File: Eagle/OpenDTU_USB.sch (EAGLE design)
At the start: 6 parts, among them M2 WIRELESS-NRF24L01-PA-EXT, X1 USBPCB

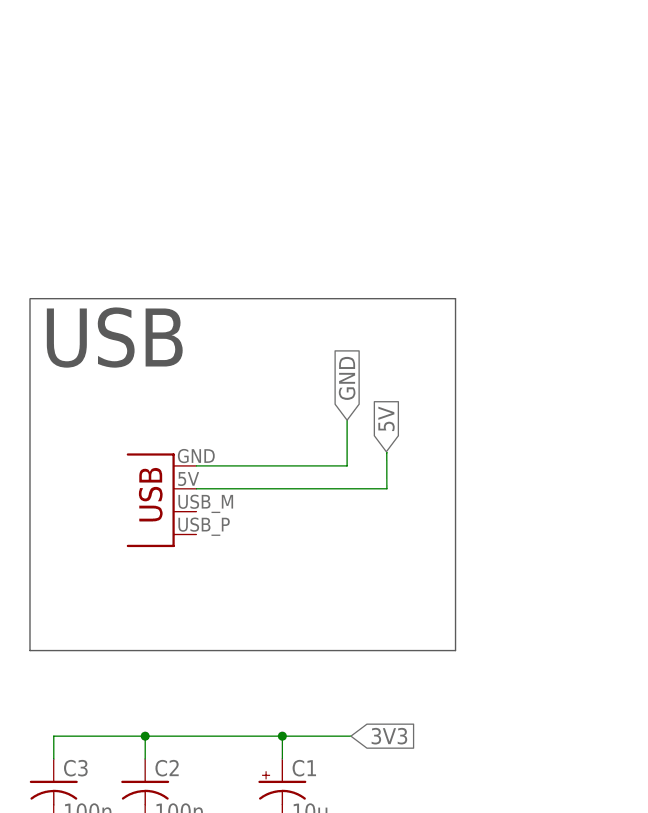
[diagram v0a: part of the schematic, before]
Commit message: Schraubklemme hinzugefügt, Empfang verbessert, USB wegbrechbar
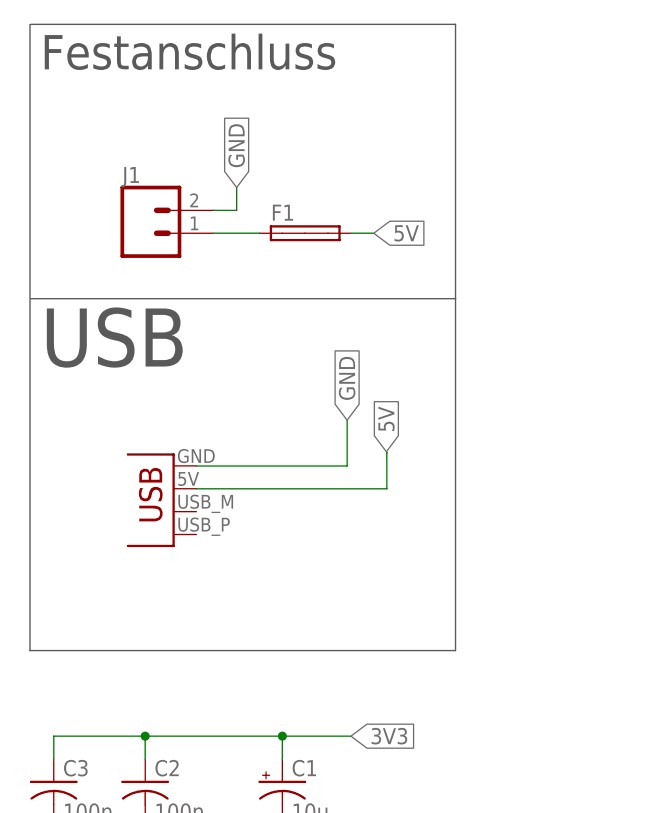
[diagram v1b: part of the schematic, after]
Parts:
- added F1: (no value), fuse:SHK20L
- added J1: (no value), SparkFun-Connectors:CONN_025MM
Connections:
- new net N$2: F1.1A, J1.1
- net 5V: now also F1.2A
- net GND: now also J1.2
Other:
- note added: "Festanschluss"
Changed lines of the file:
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@@
 <part name="C3" library="adafruit" library_urn="urn:adsk.eagle:library:420" deviceset="C-US" device="C0805K" package3d_urn="urn:adsk.eagle:package:6240397/1" value="100n"/>
 <part name="FRAME1" library="SparkFun-Aesthetics" library_urn="urn:adsk.eagle:library:507" deviceset="FRAME-A4L" device=""/>
+<part name="J1" library="SparkFun-Connectors" library_urn="urn:adsk.eagle:library:513" deviceset="CONN_02" device="5MM" package3d_urn="urn:adsk.eagle:package:38044/1"/>
+<part name="F1" library="fuse" library_urn="urn:adsk.eagle:library:233" deviceset="SHK20L" device="" package3d_urn="urn:adsk.eagle:package:14071/1"/>
 </parts>
 <sheets>
@@
 <wire x1="44.6428" y1="63.85" x2="44.6428" y2="24.75" width="0.1524" layer="97"/>
 <wire x1="44.6428" y1="24.75" x2="-2.64" y2="24.75" width="0.1524" layer="97"/>
-<wire x1="-2.64" y1="24.75" x2="-2.64" y2="63.84" width="0.1524" layer="97"/>
+<wire x1="-2.64" y1="24.75" x2="-2.64" y2="94.32" width="0.1524" layer="97"/>
 <text x="-1.46" y="56.31" size="6.4516" layer="97">USB</text>
+<wire x1="-2.53" y1="94.33" x2="44.6428" y2="94.33" width="0.1524" layer="97"/>
+<wire x1="44.6428" y1="94.33" x2="44.6428" y2="63.85" width="0.1524" layer="97"/>
+<text x="-1.46" y="89.33" size="3.81" layer="97">Festanschluss</text>
 </plain>
 <instances>
@@
 <attribute name="LAST_DATE_TIME" x="171.45" y="-77.47" size="2.286" layer="94" font="vector"/>
 <attribute name="SHEET" x="185.42" y="-82.55" size="2.54" layer="94" font="vector"/>
+</instance>
+<instance part="J1" gate="G$1" x="10.16" y="71.12" smashed="yes">
+<attribute name="VALUE" x="7.62" y="66.294" size="1.778" layer="96" font="vector"/>
+<attribute name="NAME" x="7.62" y="76.708" size="1.778" layer="95" font="vector"/>
+</instance>
+<instance part="F1" gate="G$1" x="27.94" y="71.12" smashed="yes">
+<attribute name="NAME" x="24.13" y="72.517" size="1.778" layer="95"/>
+<attribute name="VALUE" x="24.13" y="68.199" size="1.778" layer="96"/>
 </instance>
 </instances>
@@
 <junction x="10.16" y="5.08"/>
 </segment>
+<segment>
+<pinref part="J1" gate="G$1" pin="2"/>
+<wire x1="17.78" y1="73.66" x2="20.32" y2="73.66" width="0.1524" layer="91"/>
+<wire x1="20.32" y1="73.66" x2="20.32" y2="76.2" width="0.1524" layer="91"/>
+<label x="20.32" y="76.2" size="1.778" layer="95" rot="R90" xref="yes"/>
+</segment>
 </net>
 <net name="5V" class="0">
@@
 <wire x1="134.62" y1="33.02" x2="152.4" y2="33.02" width="0.1524" layer="91"/>
 <label x="152.4" y="33.02" size="1.778" layer="95" xref="yes"/>
+</segment>
+<segment>
+<pinref part="F1" gate="G$1" pin="2A"/>
+<wire x1="33.02" y1="71.12" x2="35.56" y2="71.12" width="0.1524" layer="91"/>
+<label x="35.56" y="71.12" size="1.778" layer="95" xref="yes"/>
 </segment>
 </net>
@@
 </segment>
 </net>
+<net name="N$2" class="0">
+<segment>
+<pinref part="J1" gate="G$1" pin="1"/>
+<wire x1="17.78" y1="71.12" x2="22.86" y2="71.12" width="0.1524" layer="91"/>
+<pinref part="F1" gate="G$1" pin="1A"/>
+</segment>
+</net>
